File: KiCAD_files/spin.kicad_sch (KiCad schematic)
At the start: 44 parts, among them J1 Conn_02x20_Top_Bottom, J2 Conn_01x05_Male, J3 Conn_01x06_Male, J4 Conn_01x01, J5 FTSH-107-01-F-DV-K, J6 USB_C_Receptacle_USB2.0, SW1 PTS815 SJM 250 SMTR LFS, SW2 PTS815 SJM 250 SMTR LFS, T1 Tab, T2 Tab, T3 Tab, T4 Tab, U1 STM32G474RE, U2 AZ1117-33, U3 WE-TVS-82400102, Y1 ECS-240-8-37-CKM-TR3 - 24MHz

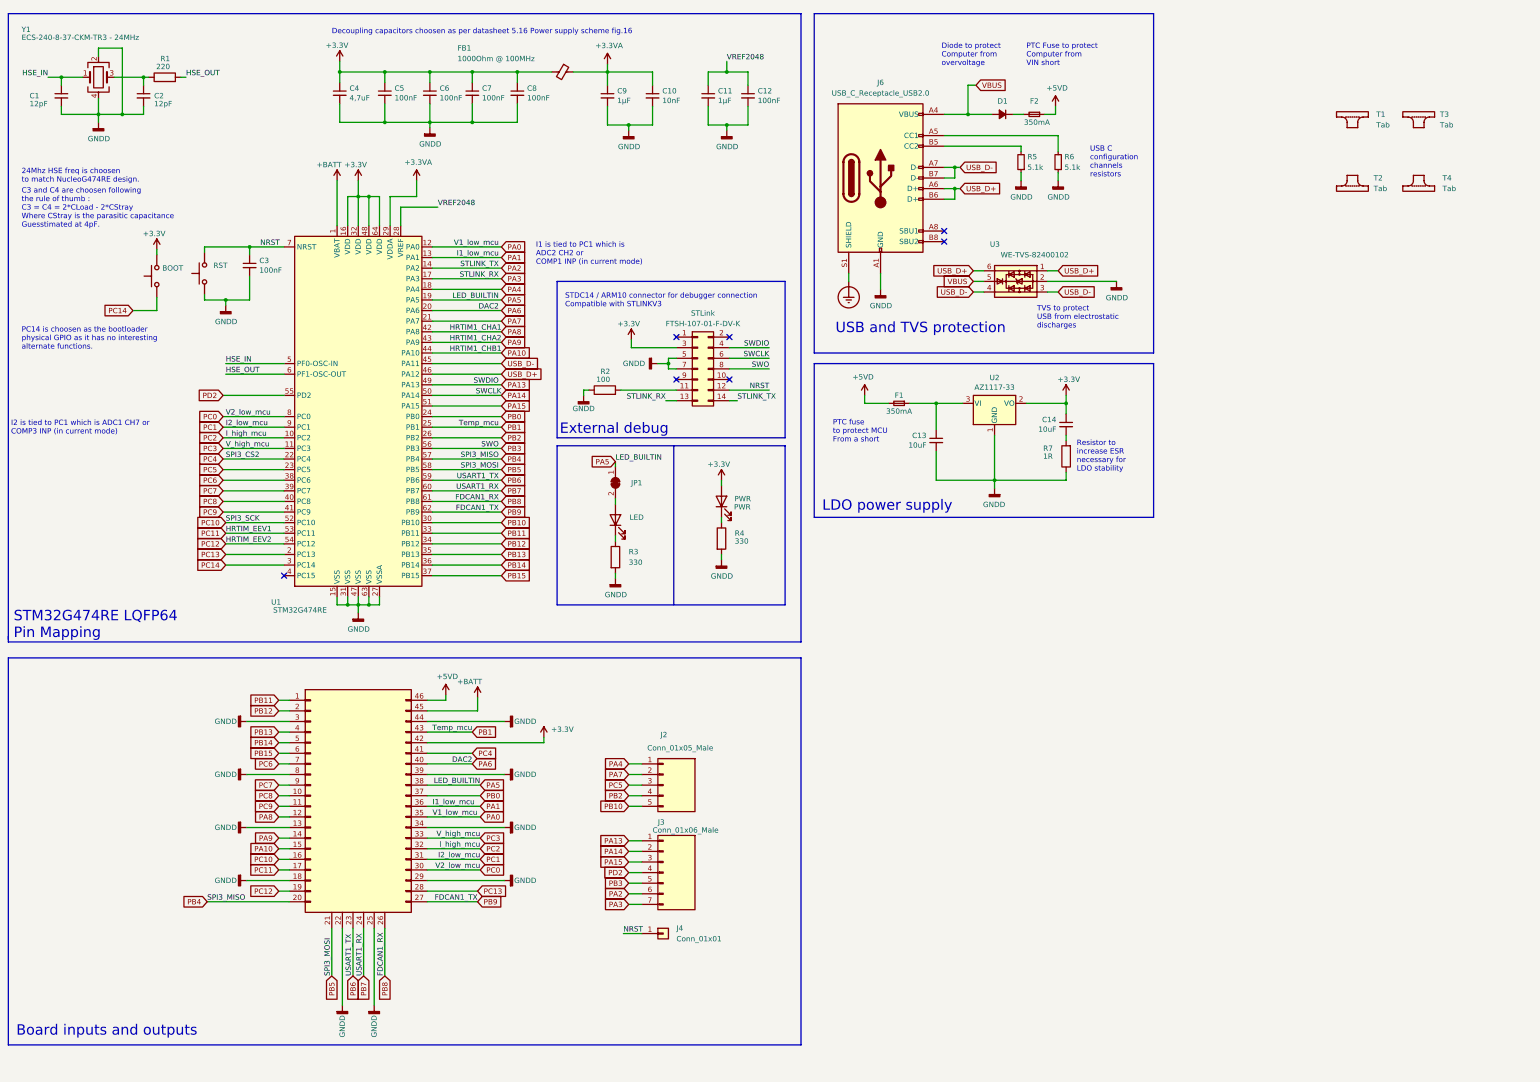
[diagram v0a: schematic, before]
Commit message: Improved Aesthetic of the schematic
Signed-off-by: Jean Alinei <jean.alinei@laas.fr>
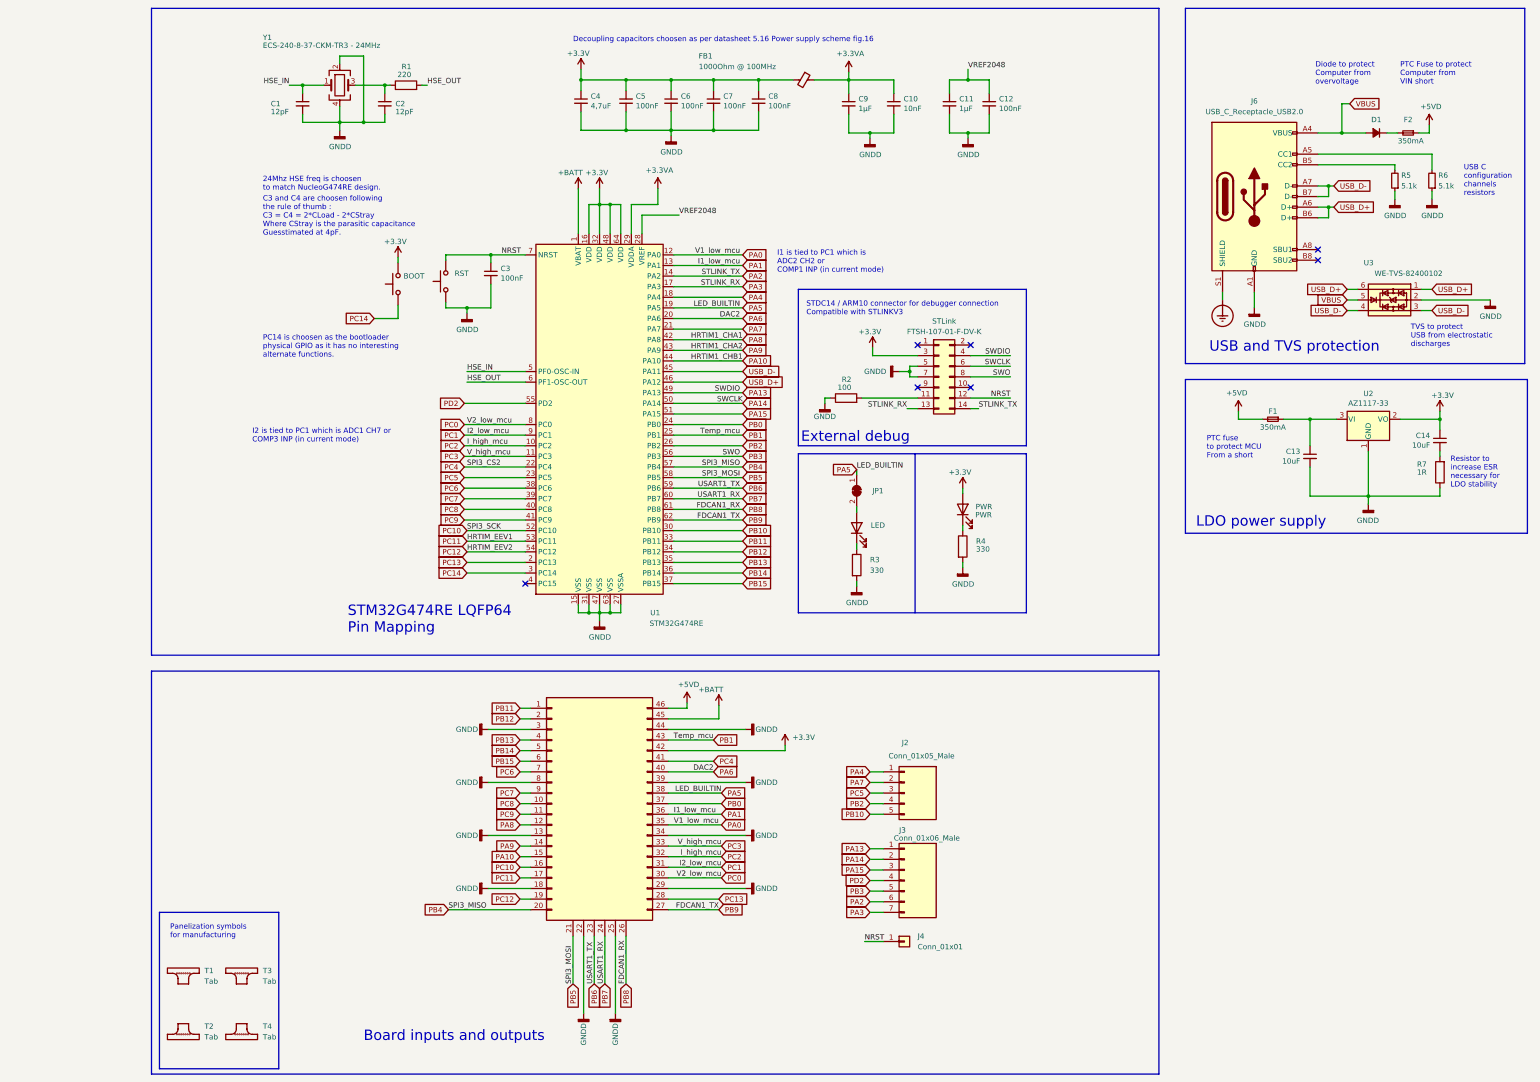
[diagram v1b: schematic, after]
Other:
- note added: "Panelization symbols for manufacturing"
- moved on the sheet: C1, C10, C11, C12, C13, C14, C2, C3, C4, C5, C6, C7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

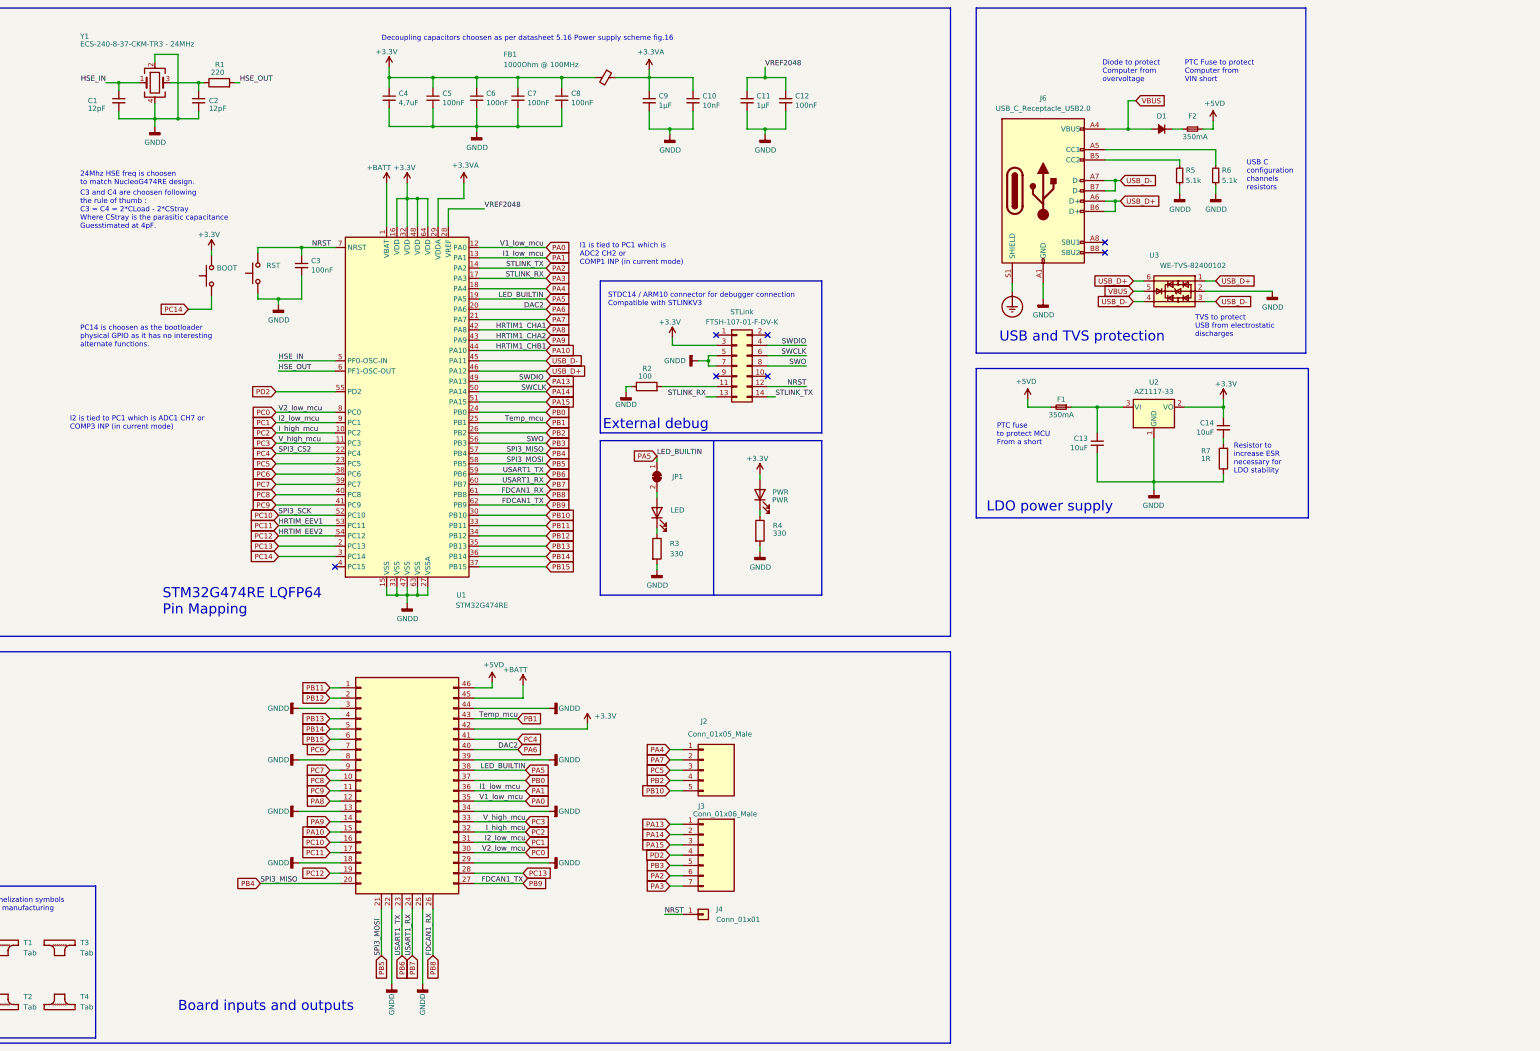
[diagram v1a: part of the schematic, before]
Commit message: Updated header layout with a proper footprint. Schematic now match firmware pinout. Warnings added for the user to notice any potential conflicts with debugger.
Signed-off-by: Jean Alinei <jean.alinei@laas.fr>
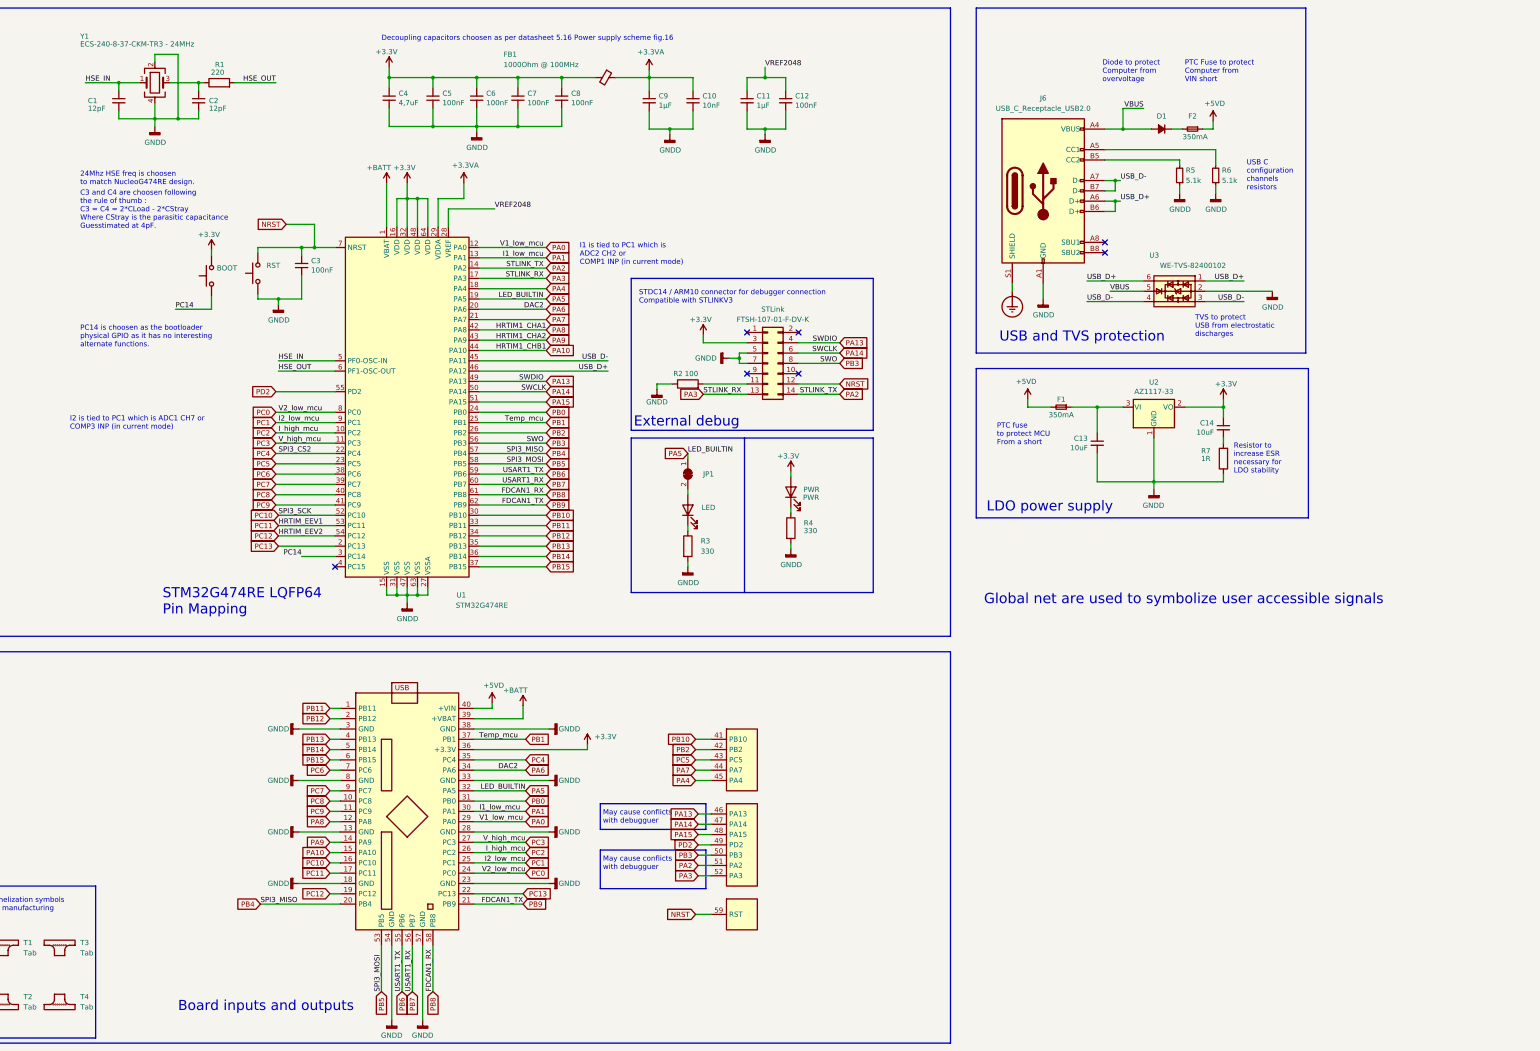
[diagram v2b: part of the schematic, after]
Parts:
- removed J1: Conn_02x20_Top_Bottom, Footprints:SPIN_castellated_holes, symbol Connector_Generic:Conn_02x20_Top_Bottom
- removed J2: Conn_01x05_Male, Footprints:PinHeader_1x05_P2.54mm_Vertical, symbol Connector:Conn_01x05_Male
- removed J3: Conn_01x06_Male, Footprints:PinHeader_1x07_P2.54mm_Vertical, symbol Connector:Conn_01x07_Male
- removed J4: Conn_01x01, Footprints:PinHeader_1x01_P2.54mm_Vertical, symbol Connector_Generic:Conn_01x01
- added J1: OwnTech_SPIN, Footprints:SPIN_castellated_holes_board, symbol Symbols:OwnTech_SPIN
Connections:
- net +3V3: now also J1.36 (+3.3V)
- net +5VD: now also J1.40 (+VIN)
- net +BATT: now also J1.39 (+VBAT)
- net GNDD: now also J1.13 (GND), J1.18 (GND), J1.23 (GND), J1.28 (GND), J1.3 (GND), J1.33 (GND), J1.38 (GND), J1.54 (GND), J1.57 (GND), J1.8 (GND)
- net NRST: now also J1.59 (RST)
- net PA0: now also J1.29 (PA0)
- net PA1: now also J1.30 (PA1)
- net PA10: now also J1.15 (PA10)
- net PA13: now also J1.46 (PA13)
- net PA14: now also J1.47 (PA14)
- net PA15: now also J1.48 (PA15)
- net PA2: now also J1.51 (PA2)
- net PA3: now also J1.52 (PA3)
- net PA4: now also J1.45 (PA4)
- net PA5: now also J1.32 (PA5)
- net PA6: now also J1.34 (PA6)
- net PA7: now also J1.44 (PA7)
- net PA8: now also J1.12 (PA8)
- net PA9: now also J1.14 (PA9)
- net PB0: now also J1.31 (PB0)
- net PB1: now also J1.37 (PB1)
- net PB10: now also J1.41 (PB10)
- net PB11: now also J1.1 (PB11)
- net PB12: now also J1.2 (PB12)
- net PB13: now also J1.4 (PB13)
- net PB14: now also J1.5 (PB14)
- net PB15: now also J1.6 (PB15)
- net PB2: now also J1.42 (PB2)
- net PB3: now also J1.50 (PB3)
- net PB4: now also J1.20 (PB4)
- net PB5: now also J1.53 (PB5)
- net PB6: now also J1.55 (PB6)
- net PB7: now also J1.56 (PB7)
- net PB8: now also J1.58 (PB8)
- net PB9: now also J1.21 (PB9)
- net PC0: now also J1.24 (PC0)
- net PC1: now also J1.25 (PC1)
- net PC10: now also J1.16 (PC10)
- net PC11: now also J1.17 (PC11)
- net PC12: now also J1.19 (PC12)
- net PC13: now also J1.22 (PC13)
- net PC2: now also J1.26 (PC2)
- net PC3: now also J1.27 (PC3)
- net PC4: now also J1.35 (PC4)
- net PC5: now also J1.43 (PC5)
- net PC6: now also J1.7 (PC6)
- net PC7: now also J1.9 (PC7)
- net PC8: now also J1.10 (PC8)
- net PC9: now also J1.11 (PC9)
- net PD2: now also J1.49 (PD2)
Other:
- note added: "Global net are used to symbolize user accessible signals"
- note added: "May cause conflicts with debugguer"
- moved on the sheet: JP1, R2, R3, R4
